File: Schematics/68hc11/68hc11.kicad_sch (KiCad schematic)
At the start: 37 parts, among them J1 DC 5 Volts, J2 DB9_Female, J3 Screw_Terminal_01x10, J4 Screw_Terminal_01x10, J5 Screw_Terminal_01x10, J6 Screw_Terminal_01x10, SW1 Reset, U1 MC68HC11A1CC-PLLC, U10 MCP100-270D, U2 MC68B21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

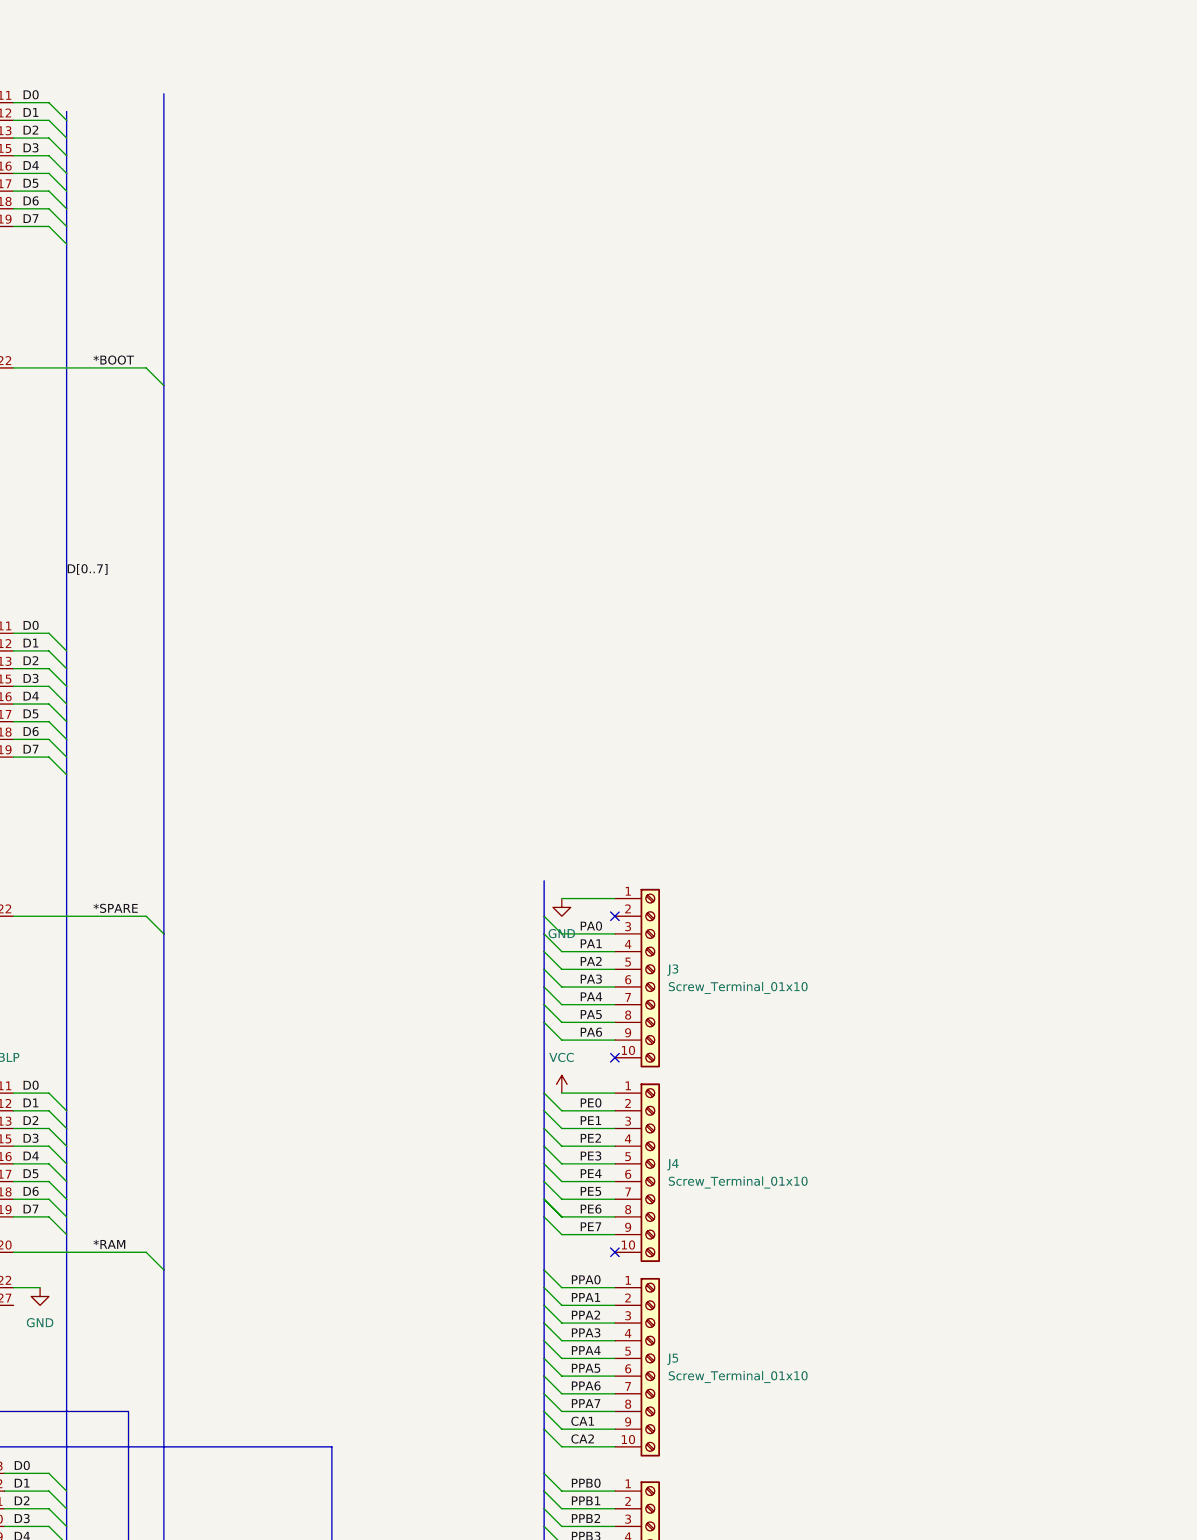
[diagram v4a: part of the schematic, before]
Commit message: Added address logic chips
Next is layout
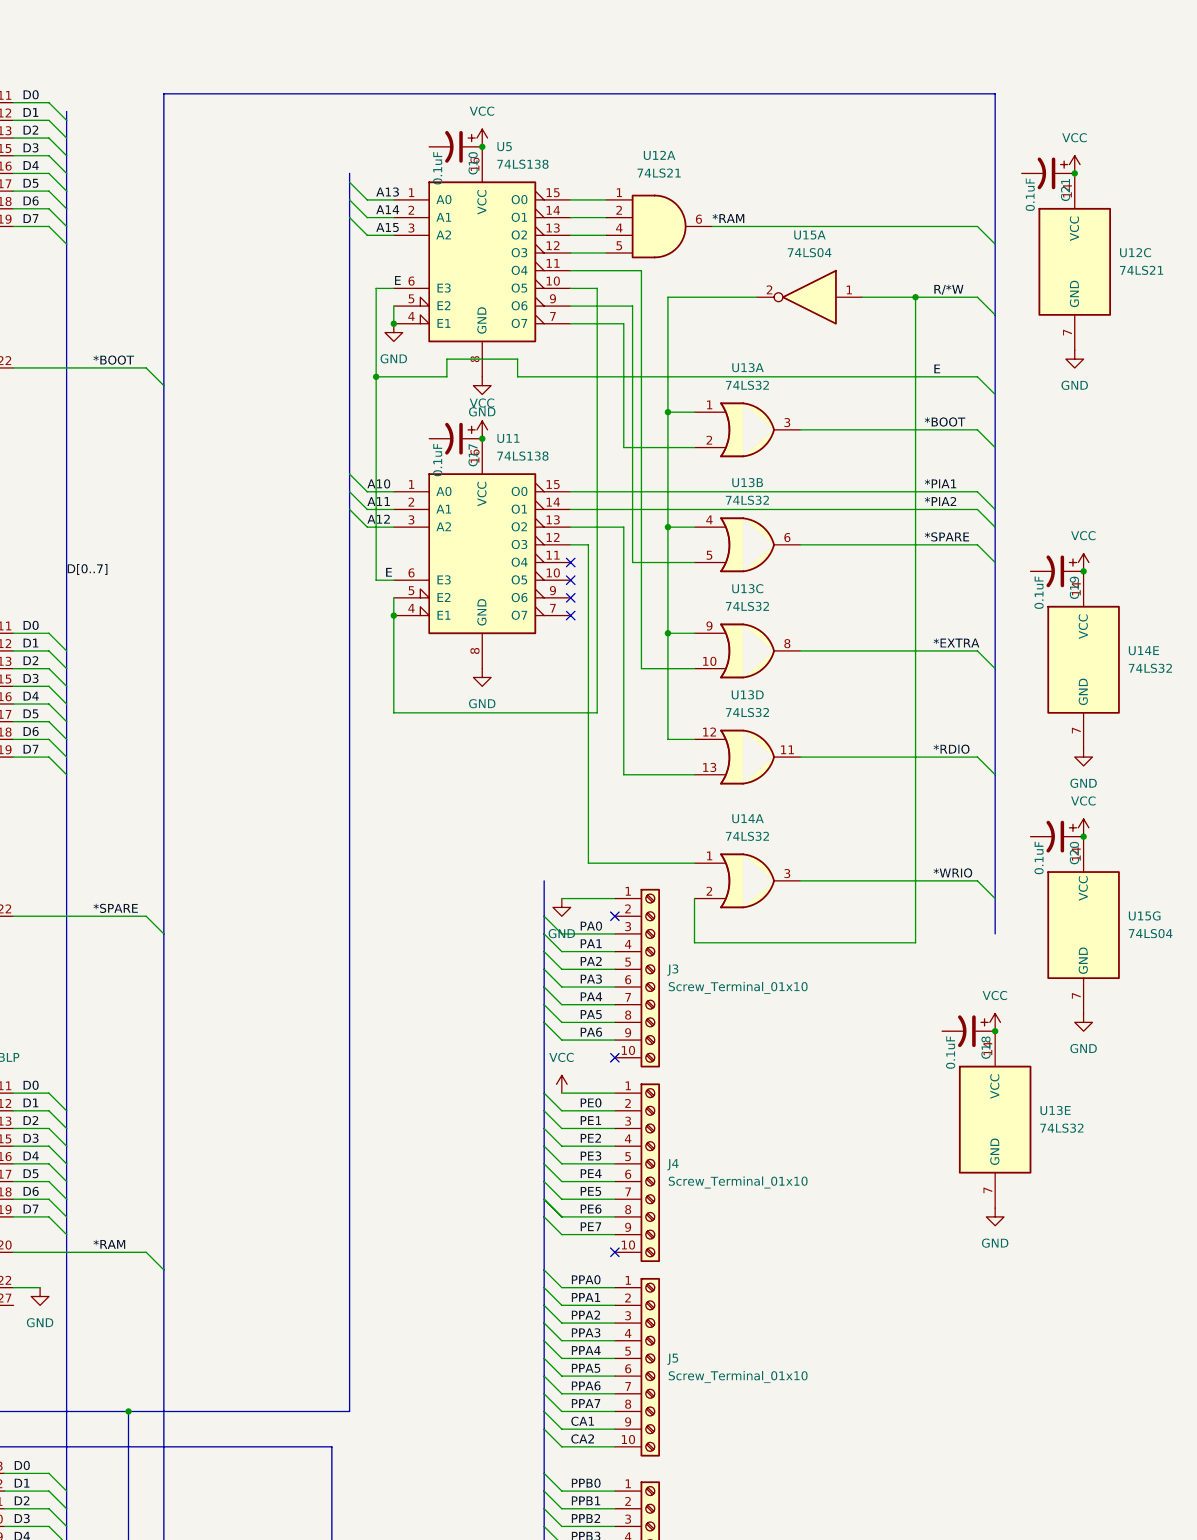
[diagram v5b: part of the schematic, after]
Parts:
- added C10, C17, C18, C19, C20, C21: 0.1uF, Capacitor_THT:C_Disc_D3.0mm_W2.0mm_P2.50mm, symbol Device:C_Polarized_US
- added U11, U5: 74LS138, Package_DIP:DIP-16_W7.62mm_Socket, symbol 74xx:74LS138
- added U12: 74LS21, Package_DIP:DIP-14_W7.62mm_Socket, symbol 74xx:74LS21
- added U13: 74LS32, symbol 74xx:74LS32
- added U14: 74LS32, Package_DIP:DIP-14_W7.62mm_Socket, symbol 74xx:74LS32
- added U15: 74LS04, Package_DIP:DIP-14_W7.62mm_Socket, symbol 74xx:74LS04
- J1: footprint Connector_BarrelJack:BarrelJack_CUI_PJ-063AH_Horizontal_CircularHoles -> digikey-footprints:Barrel_Jack_5.5mmODx2.1mmID_PJ-102A
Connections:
- net *BOOT: now also U13.3
- net *PIA1: now also U11.15 (O0)
- net *RAM: now also U12.6
- net *SPARE: now also U13.6
- net A10: now also U11.1 (A0)
- net A11: now also U11.2 (A1)
- net A12: now also U11.3 (A2)
- net A13: now also U5.1 (A0)
- net A14: now also U5.2 (A1)
- net A15: now also U5.3 (A2)
- net E: now also U11.6 (E3), U5.6 (E3)
- net GND: now also U11.8 (GND), U12.7 (GND), U13.7 (GND), U14.7 (GND), U15.7 (GND), U5.4 (E1), U5.5 (E2), U5.8 (GND)
- net R/*W: now also U14.2, U15.1
- net VCC: now also C10.1, C17.1, C18.1, C19.1, C20.1, C21.1, U11.16 (VCC), U12.14 (VCC), U13.14 (VCC), U14.14 (VCC), U15.14 (VCC), U5.16 (VCC)
- new net: U13.1, U13.12, U13.4, U13.9, U15.2
- new net: U11.13 (O2), U13.13
- new net: U11.12 (O3), U14.1
- new net: U11.4 (E1), U11.5 (E2), U5.10 (O5)
- new net: U13.10, U5.11 (O4)
- new net: U12.5, U5.12 (O3)
- new net: U12.4, U5.13 (O2)
- new net: U12.2, U5.14 (O1)
- new net: U12.1, U5.15 (O0)
- new net: U13.2, U5.7 (O7)
- new net: U13.5, U5.9 (O6)
- new net *EXTRA: U13.8
- new net *PIA2: U11.14 (O1)
- new net *RDIO: U13.11
- new net *WRIO: U14.3
- no-connect marks 10 -> 14

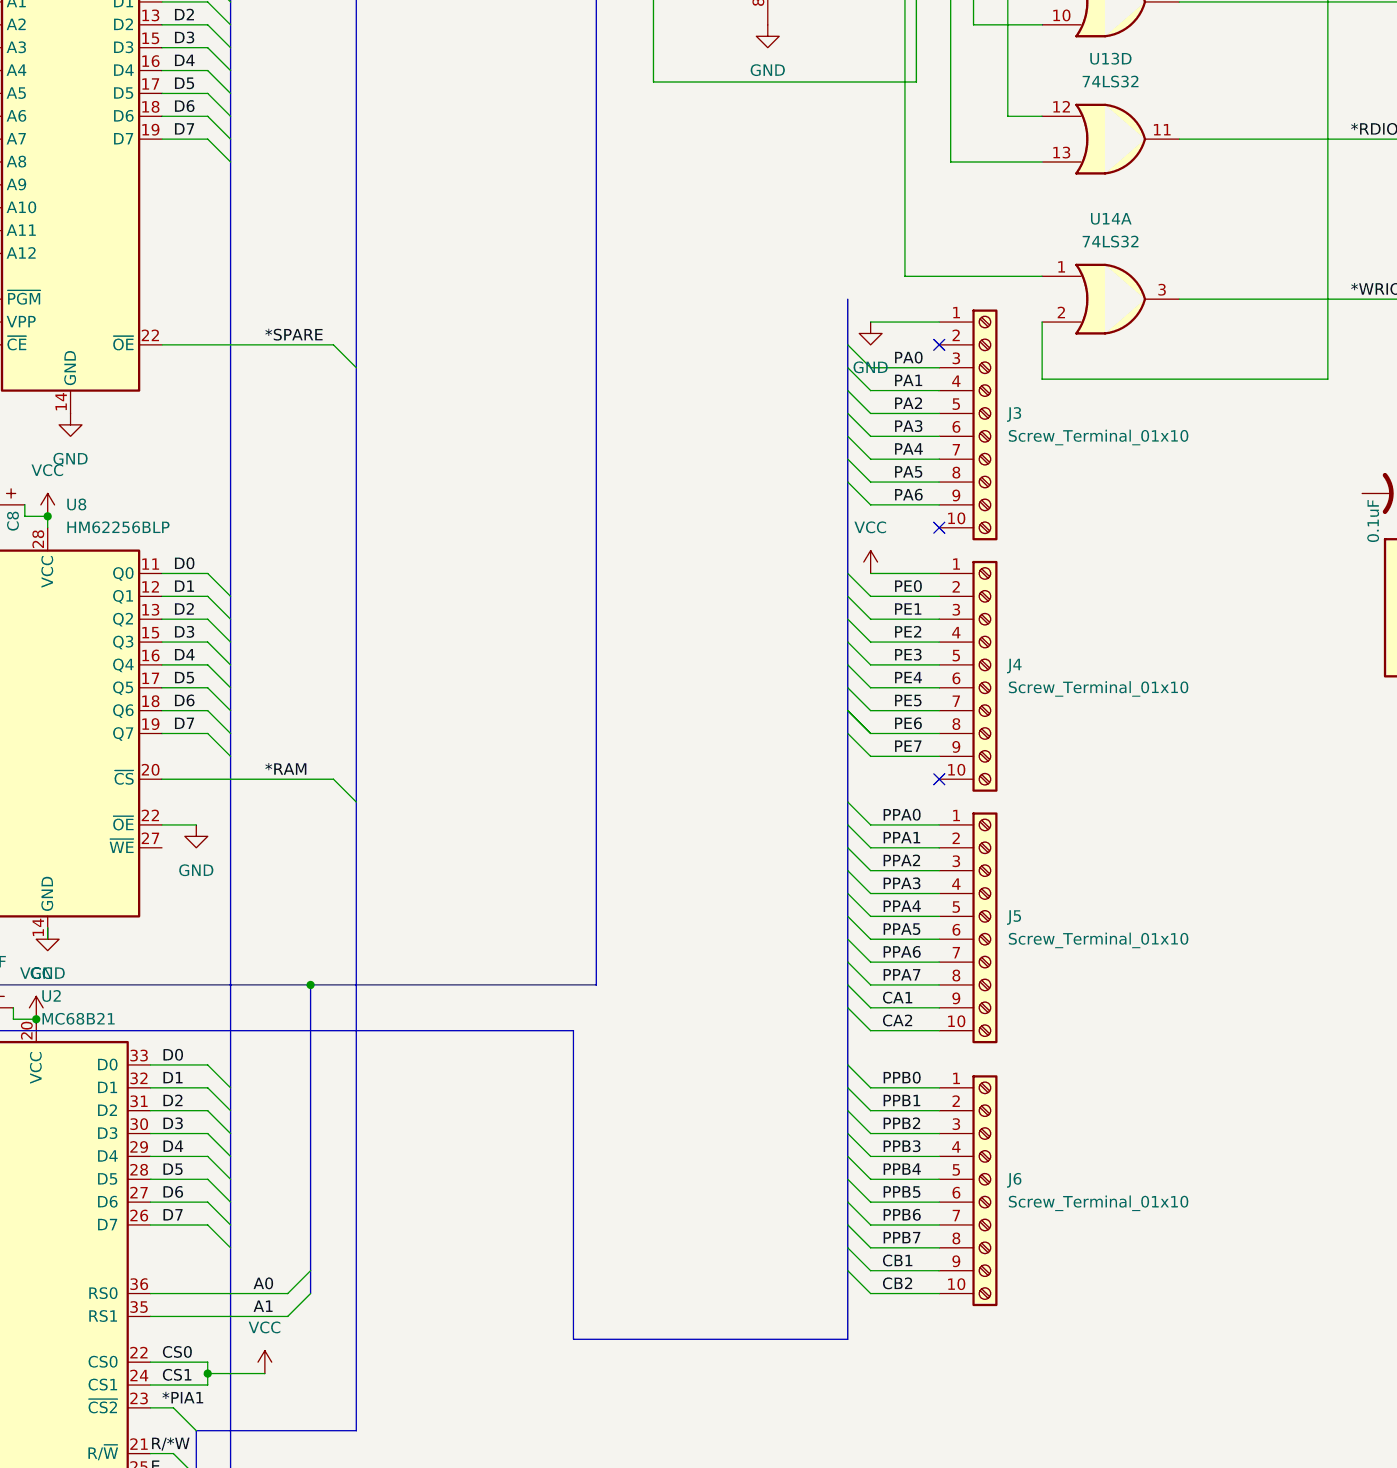
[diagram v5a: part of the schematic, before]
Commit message: Replaced screw terminals with pin headers
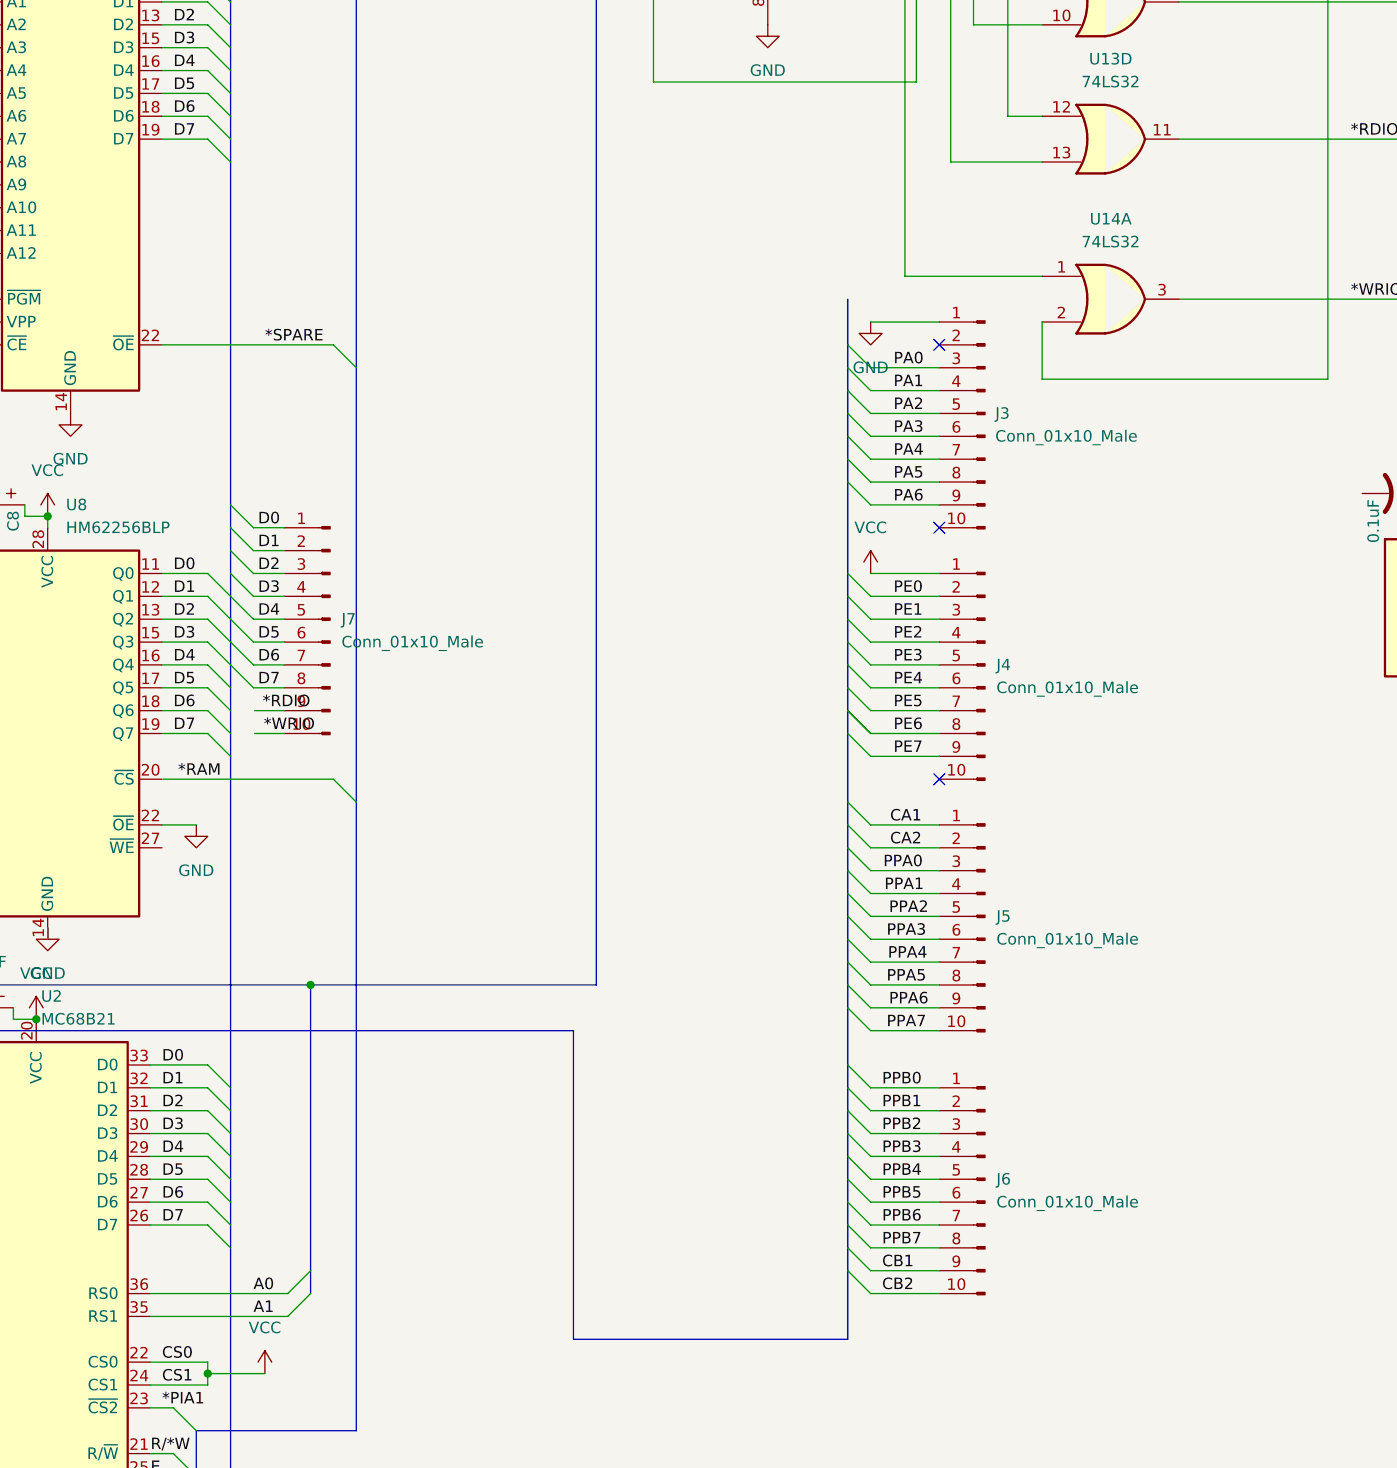
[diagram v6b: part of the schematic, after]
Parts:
- removed J3, J4, J5, J6: Screw_Terminal_01x10, TerminalBlock_4Ucon:TerminalBlock_4Ucon_1x10_P3.50mm_Horizontal, symbol Connector:Screw_Terminal_01x10
- added J3, J4, J5, J6, J7: Conn_01x10_Male, Connector_PinSocket_2.54mm:PinSocket_1x10_P2.54mm_Vertical, symbol Connector:Conn_01x10_Male
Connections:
- net *RAM: no longer U8.20 (~{CS})
- net *RDIO: now also J7.9 (Pin_9)
- net *WRIO: now also J7.10 (Pin_10)
- net CA1: now also J5.1 (Pin_1)
- net CA2: now also J5.2 (Pin_2)
- net CB1: now also J6.9 (Pin_9)
- net CB2: now also J6.10 (Pin_10)
- net D0: now also J7.1 (Pin_1)
- net D1: now also J7.2 (Pin_2)
- net D2: now also J7.3 (Pin_3)
- net D3: now also J7.4 (Pin_4)
- net D4: now also J7.5 (Pin_5)
- net D5: now also J7.6 (Pin_6)
- net D6: now also J7.7 (Pin_7)
- net D7: now also J7.8 (Pin_8)
- net GND: now also J3.1 (Pin_1)
- net PA0: now also J3.3 (Pin_3)
- net PA1: now also J3.4 (Pin_4)
- net PA2: now also J3.5 (Pin_5)
- net PA3: now also J3.6 (Pin_6)
- net PA4: now also J3.7 (Pin_7)
- net PA5: now also J3.8 (Pin_8)
- net PA6: now also J3.9 (Pin_9)
- net PE0: now also J4.2 (Pin_2)
- net PE1: now also J4.3 (Pin_3)
- net PE2: now also J4.4 (Pin_4)
- net PE3: now also J4.5 (Pin_5)
- net PE4: now also J4.6 (Pin_6)
- net PE5: now also J4.7 (Pin_7)
- net PE6: now also J4.8 (Pin_8)
- net PE7: now also J4.9 (Pin_9)
- net PPA0: now also J5.3 (Pin_3)
- net PPA1: now also J5.4 (Pin_4)
- net PPA2: now also J5.5 (Pin_5)
- net PPA3: now also J5.6 (Pin_6)
- net PPA4: now also J5.7 (Pin_7)
- net PPA5: now also J5.8 (Pin_8)
- net PPA6: now also J5.9 (Pin_9)
- net PPA7: now also J5.10 (Pin_10)
- net PPB0: now also J6.1 (Pin_1)
- net PPB1: now also J6.2 (Pin_2)
- net PPB2: now also J6.3 (Pin_3)
- net PPB3: now also J6.4 (Pin_4)
- net PPB4: now also J6.5 (Pin_5)
- net PPB5: now also J6.6 (Pin_6)
- net PPB6: now also J6.7 (Pin_7)
- net PPB7: now also J6.8 (Pin_8)
- net VCC: now also J4.1 (Pin_1)
